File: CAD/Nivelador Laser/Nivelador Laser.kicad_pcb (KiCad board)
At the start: 2 copper layers, 8 parts

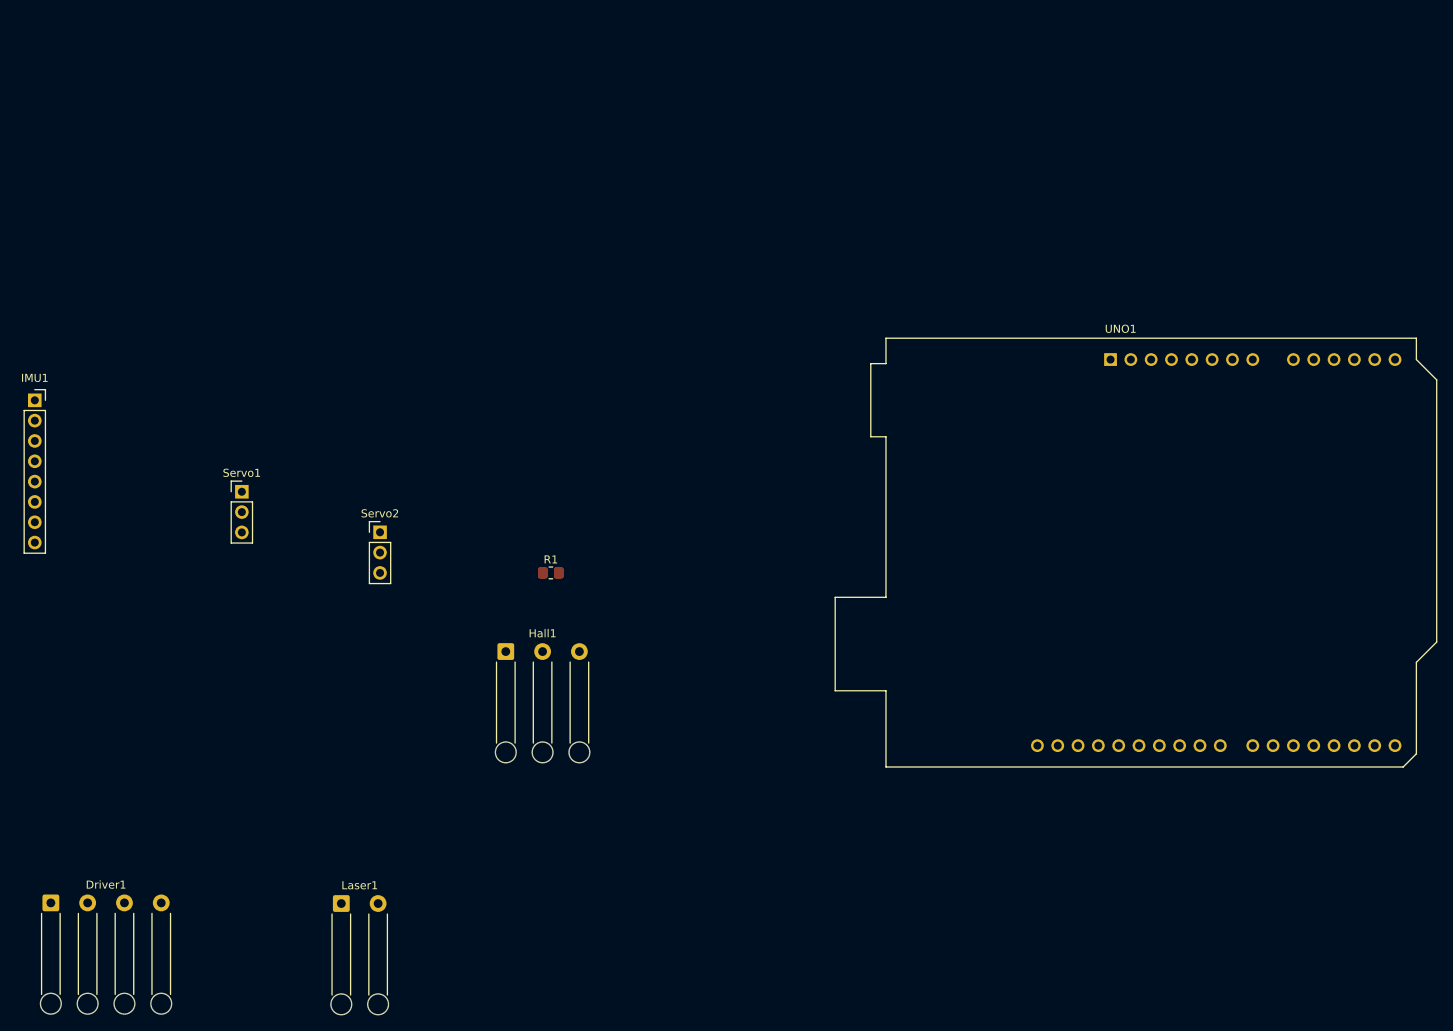
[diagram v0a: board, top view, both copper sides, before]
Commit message: added laser reciever
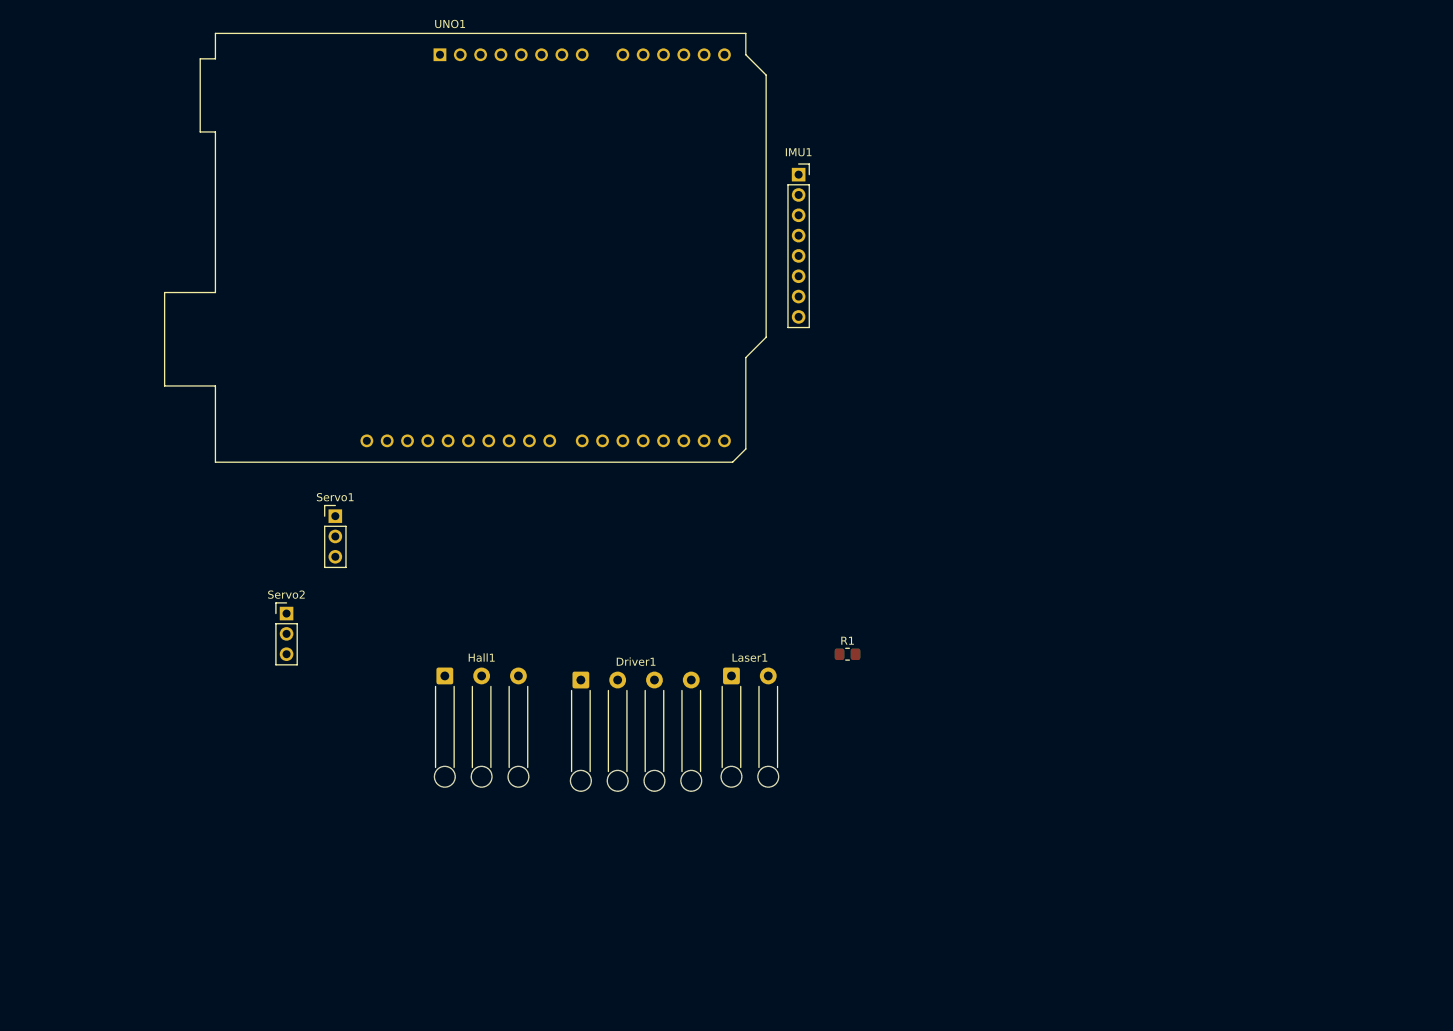
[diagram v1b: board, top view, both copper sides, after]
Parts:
- moved IMU1 99.6 mm to (152.9, 42.2)
- moved UNO1 92.1 mm to (108.1, 27.2)
- moved Driver1 71.9 mm to (125.7, 105.3)
- moved Laser1 56.5 mm to (144.5, 104.8)
- moved R1 38.5 mm to (159.0, 102.1)
- moved Servo2 15.5 mm to (88.9, 97.0)
- moved Servo1 12.1 mm to (95.0, 84.9)
- moved Hall1 8.21 mm to (108.7, 104.8)
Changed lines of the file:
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@@
 	)
 	(setup
+		(stackup
+			(layer "F.SilkS"
+				(type "Top Silk Screen")
+			)
+			(layer "F.Paste"
+				(type "Top Solder Paste")
+			)
+			(layer "F.Mask"
+				(type "Top Solder Mask")
+				(thickness 0.01)
+			)
+			(layer "F.Cu"
+				(type "copper")
+				(thickness 0.035)
+			)
+			(layer "dielectric 1"
+				(type "core")
+				(thickness 1.51)
+				(material "FR4")
+				(epsilon_r 4.5)
+				(loss_tangent 0.02)
+			)
+			(layer "B.Cu"
+				(type "copper")
+				(thickness 0.035)
+			)
+			(layer "B.Mask"
+				(type "Bottom Solder Mask")
+				(thickness 0.01)
+			)
+			(layer "B.Paste"
+				(type "Bottom Solder Paste")
+			)
+			(layer "B.SilkS"
+				(type "Bottom Silk Screen")
+			)
+			(copper_finish "None")
+			(dielectric_constraints no)
+		)
 		(pad_to_mask_clearance 0)
 		(allow_soldermask_bridges_in_footprints no)
@@
 	(footprint "Connector_PinHeader_2.54mm:PinHeader_1x03_P2.54mm_Vertical"
 		(layer "F.Cu")
-		(at 100.584 86.868)
+		(at 88.9 97.028)
 		(descr "Through hole straight pin header, 1x03, 2.54mm pitch, single row")
 		(tags "Through hole pin header THT 1x03 2.54mm single row")
@@
 	(footprint "Connector_Wire:SolderWire-0.5sqmm_1x04_P4.6mm_D0.9mm_OD2.1mm_Relief"
 		(layer "F.Cu")
-		(at 59.436 133.196)
+		(at 125.688 105.335)
 		(descr "Soldered wire connection with feed through strain relief, for 4 times 0.5 mm² wires, basic insulation, conductor diameter 0.9mm, outer diameter 2.1mm, size source Multi-Contact FLEXI-E 0.5 (https://ec.staubli.com/AcroFiles/Catalogues/TM_Cab-Main-11014119_(en)_hi.pdf), bend radius 3 times outer diameter, generated with kicad-footprint-generator")
 		(tags "connector wire 0.5sqmm strain-relief")
@@
 	(footprint "Connector_Wire:SolderWire-0.5sqmm_1x03_P4.6mm_D0.9mm_OD2.1mm_Relief"
 		(layer "F.Cu")
-		(at 116.304 101.779)
+		(at 108.684 104.827)
 		(descr "Soldered wire connection with feed through strain relief, for 3 times 0.5 mm² wires, basic insulation, conductor diameter 0.9mm, outer diameter 2.1mm, size source Multi-Contact FLEXI-E 0.5 (https://ec.staubli.com/AcroFiles/Catalogues/TM_Cab-Main-11014119_(en)_hi.pdf), bend radius 3 times outer diameter, generated with kicad-footprint-generator")
 		(tags "connector wire 0.5sqmm strain-relief")
@@
 	(footprint "Connector_Wire:SolderWire-0.5sqmm_1x02_P4.6mm_D0.9mm_OD2.1mm_Relief"
 		(layer "F.Cu")
-		(at 95.744 133.275)
+		(at 144.512 104.827)
 		(descr "Soldered wire connection with feed through strain relief, for 2 times 0.5 mm² wires, basic insulation, conductor diameter 0.9mm, outer diameter 2.1mm, size source Multi-Contact FLEXI-E 0.5 (https://ec.staubli.com/AcroFiles/Catalogues/TM_Cab-Main-11014119_(en)_hi.pdf), bend radius 3 times outer diameter, generated with kicad-footprint-generator")
 		(tags "connector wire 0.5sqmm strain-relief")
@@
 	(footprint "Module:Arduino_UNO_R3"
 		(layer "F.Cu")
-		(at 191.897 65.278)
+		(at 108.077 27.178)
 		(descr "Arduino UNO R3, http://www.mouser.com/pdfdocs/Gravitech_Arduino_Nano3_0.pdf")
 		(tags "Arduino UNO R3")
@@
 	(footprint "Resistor_SMD:R_0805_2012Metric_Pad1.20x1.40mm_HandSolder"
 		(layer "F.Cu")
-		(at 121.936 91.948)
+		(at 159.02 102.108)
 		(descr "Resistor SMD 0805 (2012 Metric), square (rectangular) end terminal, IPC_7351 nominal with elongated pad for handsoldering. (Body size source: IPC-SM-782 page 72, https://www.pcb-3d.com/wordpress/wp-content/uploads/ipc-sm-782a_amendment_1_and_2.pdf), generated with kicad-footprint-generator")
 		(tags "resistor handsolder")
@@
 	(footprint "Connector_PinSocket_2.54mm:PinSocket_1x08_P2.54mm_Vertical"
 		(layer "F.Cu")
-		(at 57.429 70.373)
+		(at 152.908 42.164)
 		(descr "Through hole straight socket strip, 1x08, 2.54mm pitch, single row (from Kicad 4.0.7), script generated")
 		(tags "Through hole socket strip THT 1x08 2.54mm single row")
@@
 	(footprint "Connector_PinHeader_2.54mm:PinHeader_1x03_P2.54mm_Vertical"
 		(layer "F.Cu")
-		(at 83.312 81.803)
+		(at 94.996 84.851)
 		(descr "Through hole straight pin header, 1x03, 2.54mm pitch, single row")
 		(tags "Through hole pin header THT 1x03 2.54mm single row")

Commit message: changes
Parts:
- moved R1 94.2 mm to (75.0, 59.5)
- moved Driver1 42.6 mm to (166.6, 117.1)
- moved IMU1 37.8 mm to (184.0, 63.6)
- moved UNO1 36.9 mm to (138.3, 48.4)
- moved Laser1 4.82 mm to (140.5, 107.5)
- moved Servo1 4.07 mm to (95.0, 88.9)
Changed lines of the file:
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@@
 	(footprint "Connector_Wire:SolderWire-0.5sqmm_1x04_P4.6mm_D0.9mm_OD2.1mm_Relief"
 		(layer "F.Cu")
-		(at 125.688 105.335)
+		(at 166.6 117.075)
 		(descr "Soldered wire connection with feed through strain relief, for 4 times 0.5 mm² wires, basic insulation, conductor diameter 0.9mm, outer diameter 2.1mm, size source Multi-Contact FLEXI-E 0.5 (https://ec.staubli.com/AcroFiles/Catalogues/TM_Cab-Main-11014119_(en)_hi.pdf), bend radius 3 times outer diameter, generated with kicad-footprint-generator")
 		(tags "connector wire 0.5sqmm strain-relief")
@@
 	(footprint "Connector_Wire:SolderWire-0.5sqmm_1x02_P4.6mm_D0.9mm_OD2.1mm_Relief"
 		(layer "F.Cu")
-		(at 144.512 104.827)
+		(at 140.5 107.5)
 		(descr "Soldered wire connection with feed through strain relief, for 2 times 0.5 mm² wires, basic insulation, conductor diameter 0.9mm, outer diameter 2.1mm, size source Multi-Contact FLEXI-E 0.5 (https://ec.staubli.com/AcroFiles/Catalogues/TM_Cab-Main-11014119_(en)_hi.pdf), bend radius 3 times outer diameter, generated with kicad-footprint-generator")
 		(tags "connector wire 0.5sqmm strain-relief")
@@
 	(footprint "Module:Arduino_UNO_R3"
 		(layer "F.Cu")
-		(at 108.077 27.178)
+		(at 138.325 48.37)
 		(descr "Arduino UNO R3, http://www.mouser.com/pdfdocs/Gravitech_Arduino_Nano3_0.pdf")
 		(tags "Arduino UNO R3")
@@
 			(net 26 "unconnected-(UNO1-IOREF-Pad2)")
 			(pinfunction "IOREF")
-			(pintype "output")
+			(pintype "output+no_connect")
 		)
 		(pad "3" thru_hole oval
@@
 			(net 35 "unconnected-(UNO1-~{RESET}-Pad3)")
 			(pinfunction "~{RESET}")
-			(pintype "input")
+			(pintype "input+no_connect")
 		)
 		(pad "4" thru_hole oval
@@
 			(net 23 "unconnected-(UNO1-3V3-Pad4)")
 			(pinfunction "3V3")
-			(pintype "power_out")
+			(pintype "power_out+no_connect")
 		)
 		(pad "5" thru_hole oval
@@
 			(net 30 "unconnected-(UNO1-VIN-Pad8)")
 			(pinfunction "VIN")
-			(pintype "power_in")
+			(pintype "power_in+no_connect")
 		)
 		(pad "9" thru_hole oval
@@
 			(net 22 "unconnected-(UNO1-A0-Pad9)")
 			(pinfunction "A0")
-			(pintype "bidirectional")
+			(pintype "bidirectional+no_connect")
 		)
 		(pad "10" thru_hole oval
@@
 			(net 15 "unconnected-(UNO1-A1-Pad10)")
 			(pinfunction "A1")
-			(pintype "bidirectional")
+			(pintype "bidirectional+no_connect")
 		)
 		(pad "11" thru_hole oval
@@
 			(net 32 "unconnected-(UNO1-A2-Pad11)")
 			(pinfunction "A2")
-			(pintype "bidirectional")
+			(pintype "bidirectional+no_connect")
 		)
 		(pad "12" thru_hole oval
@@
 			(net 17 "unconnected-(UNO1-A3-Pad12)")
 			(pinfunction "A3")
-			(pintype "bidirectional")
+			(pintype "bidirectional+no_connect")
 		)
 		(pad "13" thru_hole oval
@@
 			(net 33 "unconnected-(UNO1-D0{slash}RX-Pad15)")
 			(pinfunction "D0/RX")
-			(pintype "bidirectional")
+			(pintype "bidirectional+no_connect")
 		)
 		(pad "16" thru_hole oval
@@
 			(net 29 "unconnected-(UNO1-D1{slash}TX-Pad16)")
 			(pinfunction "D1/TX")
-			(pintype "bidirectional")
+			(pintype "bidirectional+no_connect")
 		)
 		(pad "17" thru_hole oval
@@
 			(net 31 "unconnected-(UNO1-D2-Pad17)")
 			(pinfunction "D2")
-			(pintype "bidirectional")
+			(pintype "bidirectional+no_connect")
 		)
 		(pad "18" thru_hole oval
@@
 			(net 19 "unconnected-(UNO1-D3-Pad18)")
 			(pinfunction "D3")
-			(pintype "bidirectional")
+			(pintype "bidirectional+no_connect")
 		)
 		(pad "19" thru_hole oval
@@
 			(net 27 "unconnected-(UNO1-D4-Pad19)")
 			(pinfunction "D4")
-			(pintype "bidirectional")
+			(pintype "bidirectional+no_connect")
 		)
 		(pad "20" thru_hole oval
@@
 			(net 20 "unconnected-(UNO1-D10-Pad25)")
 			(pinfunction "D10")
-			(pintype "bidirectional")
+			(pintype "bidirectional+no_connect")
 		)
 		(pad "26" thru_hole oval
@@
 			(net 21 "unconnected-(UNO1-D11-Pad26)")
 			(pinfunction "D11")
-			(pintype "bidirectional")
+			(pintype "bidirectional+no_connect")
 		)
 		(pad "27" thru_hole oval
@@
 			(net 18 "unconnected-(UNO1-D12-Pad27)")
 			(pinfunction "D12")
-			(pintype "bidirectional")
+			(pintype "bidirectional+no_connect")
 		)
 		(pad "28" thru_hole oval
@@
 			(net 24 "unconnected-(UNO1-D13-Pad28)")
 			(pinfunction "D13")
-			(pintype "bidirectional")
+			(pintype "bidirectional+no_connect")
 		)
 		(pad "29" thru_hole oval
@@
 			(net 28 "unconnected-(UNO1-AREF-Pad30)")
 			(pinfunction "AREF")
-			(pintype "input")
+			(pintype "input+no_connect")
 		)
 		(pad "31" thru_hole oval
@@
 			(net 34 "unconnected-(UNO1-SDA{slash}A4-Pad31)")
 			(pinfunction "SDA/A4")
-			(pintype "bidirectional")
+			(pintype "bidirectional+no_connect")
 		)
 		(pad "32" thru_hole oval
@@
 			(net 16 "unconnected-(UNO1-SCL{slash}A5-Pad32)")
 			(pinfunction "SCL/A5")
-			(pintype "bidirectional")
+			(pintype "bidirectional+no_connect")
 		)
 		(model "${KICAD8_3DMODEL_DIR}/Module.3dshapes/Arduino_UNO_R3.wrl"
@@
 	(footprint "Resistor_SMD:R_0805_2012Metric_Pad1.20x1.40mm_HandSolder"
 		(layer "F.Cu")
-		(at 159.02 102.108)
+		(at 75 59.5)
 		(descr "Resistor SMD 0805 (2012 Metric), square (rectangular) end terminal, IPC_7351 nominal with elongated pad for handsoldering. (Body size source: IPC-SM-782 page 72, https://www.pcb-3d.com/wordpress/wp-content/uploads/ipc-sm-782a_amendment_1_and_2.pdf), generated with kicad-footprint-generator")
 		(tags "resistor handsolder")
@@
 	(footprint "Connector_PinSocket_2.54mm:PinSocket_1x08_P2.54mm_Vertical"
 		(layer "F.Cu")
-		(at 152.908 42.164)
+		(at 184.025 63.625)
 		(descr "Through hole straight socket strip, 1x08, 2.54mm pitch, single row (from Kicad 4.0.7), script generated")
 		(tags "Through hole socket strip THT 1x08 2.54mm single row")
@@
 	(footprint "Connector_PinHeader_2.54mm:PinHeader_1x03_P2.54mm_Vertical"
 		(layer "F.Cu")
-		(at 94.996 84.851)
+		(at 95 88.92)
 		(descr "Through hole straight pin header, 1x03, 2.54mm pitch, single row")
 		(tags "Through hole pin header THT 1x03 2.54mm single row")

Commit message: a
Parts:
- removed Driver1: Motor_Driver, Connector_Wire:SolderWire-0.5sqmm_1x04_P4.6mm_D0.9mm_OD2.1mm_Relief
- removed Hall1: Hall_Sensor, Connector_Wire:SolderWire-0.5sqmm_1x03_P4.6mm_D0.9mm_OD2.1mm_Relief
- removed R1: 10k, Resistor_SMD:R_0805_2012Metric_Pad1.20x1.40mm_HandSolder
- IMU1: footprint Connector_PinSocket_2.54mm:PinSocket_1x08_P2.54mm_Vertical -> Connector_PinSocket_2.54mm:PinSocket_1x04_P2.54mm_Vertical
- Laser1, UNO1: moved to B.Cu
- moved Servo2 96.7 mm to (175.9, 54.9)
- moved Servo1 81.3 mm to (176.1, 83.7)
- moved UNO1 55.1 mm to (166.0, 96.0)
- moved Laser1 44.3 mm to (162.9, 69.3), turned to -90 degrees
- moved IMU1 5.08 mm to (187.2, 67.6)
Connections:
- UNO1 pad 23: /HALL -> unconnected-(UNO1-D8-Pad23)
- UNO1 pad 24: /MTR -> unconnected-(UNO1-D9-Pad24)
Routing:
- net +5V: track 0.00 -> 74.3 mm
- net /SV1: track 0.00 -> 41.2 mm
- net /LSR: track 0.00 -> 36.0 mm
- net /IMU_SCL: track 0.00 -> 31.1 mm
- net /IMU_SDA: track 0.00 -> 27.2 mm
- net /SV2: track 0.00 -> 14.7 mm
- added copper zone on B.Cu, net GND
- added copper zone on F.Cu, net GND
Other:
- board outline added: 54.1 x 57.9 mm
